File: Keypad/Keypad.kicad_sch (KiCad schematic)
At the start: 3 parts, among them J1 addon_conn

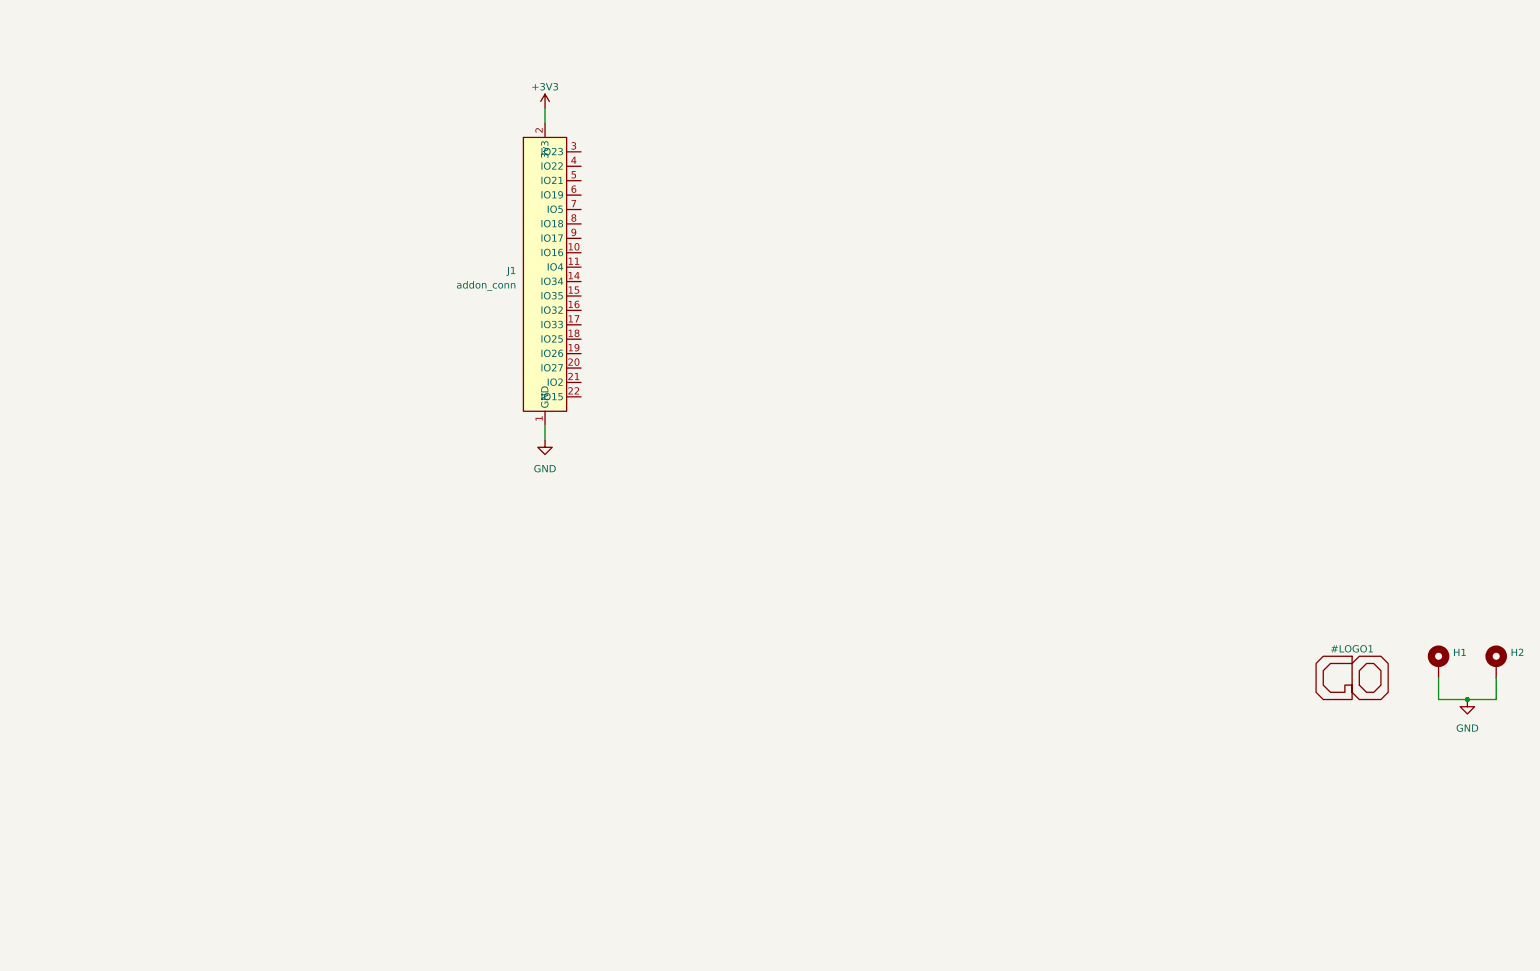
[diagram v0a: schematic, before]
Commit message: Adds schematics for keypad
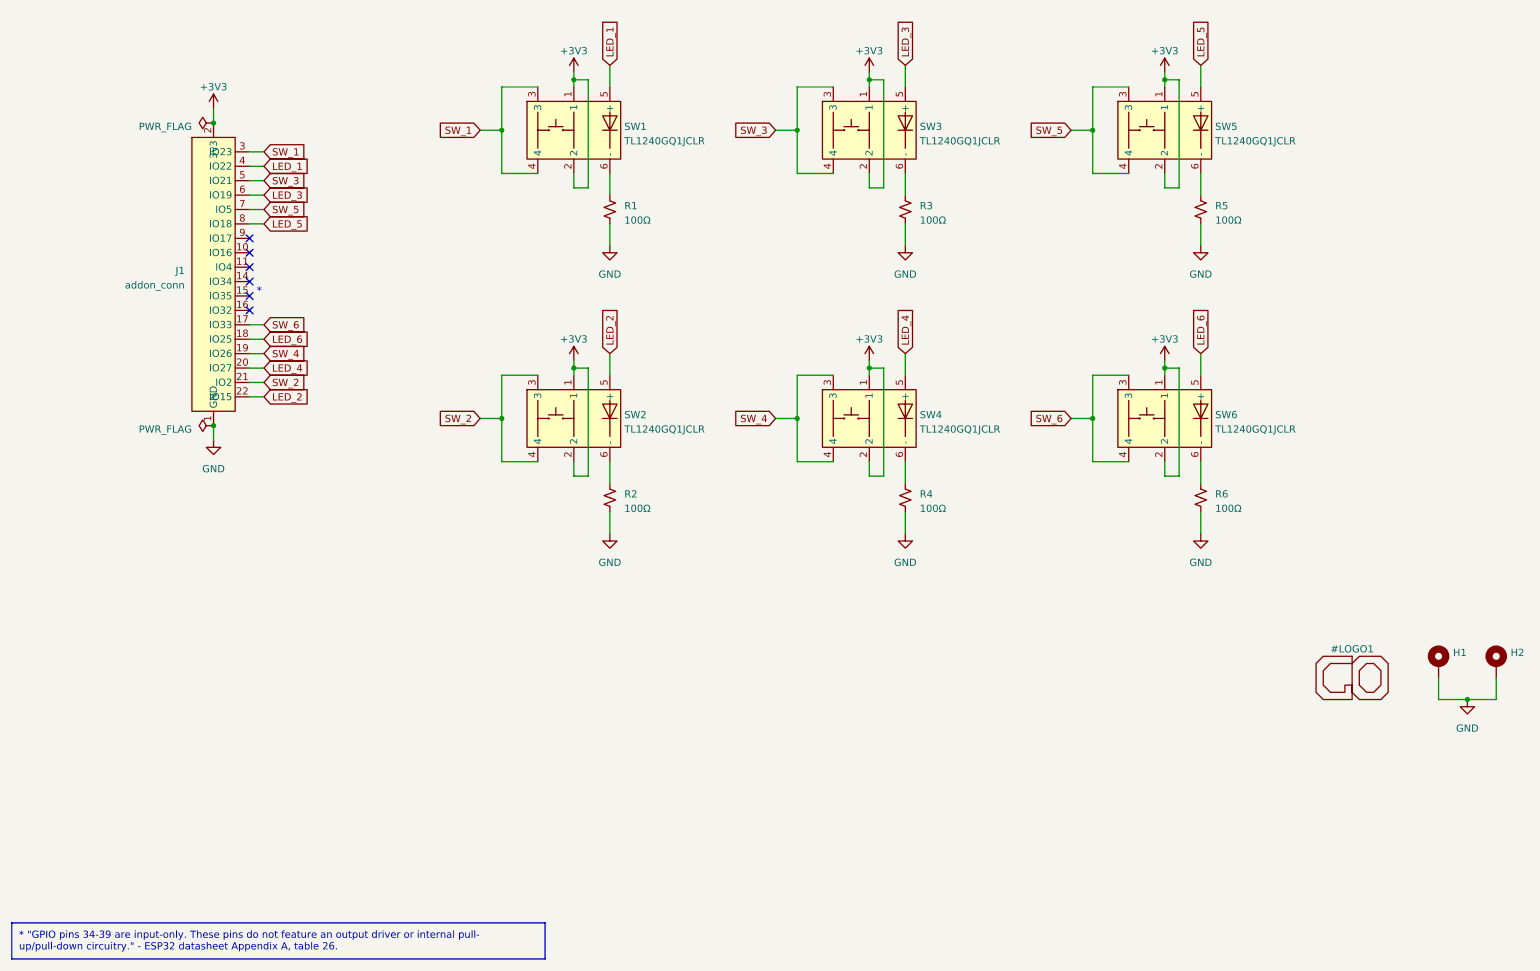
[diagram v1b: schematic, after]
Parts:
- added R1, R2, R3, R4, R5, R6: 100Ω, symbol Device:R_Small_US
- added SW1, SW2, SW3, SW4, SW5, SW6: TL1240GQ1JCLR, GameOver:TL1240GQ1JCLR, symbol GameOver:TL1240GQ1JCLR
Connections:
- net +3V3: now also SW1.1, SW1.2, SW2.1, SW2.2, SW3.1, SW3.2, SW4.1, SW4.2, SW5.1, SW5.2, SW6.1, SW6.2
- net GND: now also R1.2, R2.2, R3.2, R4.2, R5.2, R6.2
- net SW_6: now reaches J1.17 (IO33)
- net SW_6: now also SW6.3, SW6.4
- net LED_6: now reaches J1.18 (IO25)
- net LED_6: now also SW6.5 (+)
- net SW_4: now reaches J1.19 (IO26)
- net SW_4: now also SW4.3, SW4.4
- net LED_4: now reaches J1.20 (IO27)
- net LED_4: now also SW4.5 (+)
- net SW_2: now reaches J1.21 (IO2)
- net SW_2: now also SW2.3, SW2.4
- net LED_2: now reaches J1.22 (IO15)
- net LED_2: now also SW2.5 (+)
- net SW_1: now reaches J1.3 (IO23)
- net SW_1: now also SW1.3, SW1.4
- net LED_1: now reaches J1.4 (IO22)
- net LED_1: now also SW1.5 (+)
- net SW_3: now reaches J1.5 (IO21)
- net SW_3: now also SW3.3, SW3.4
- net LED_3: now reaches J1.6 (IO19)
- net LED_3: now also SW3.5 (+)
- net SW_5: now reaches J1.7 (IO5)
- net SW_5: now also SW5.3, SW5.4
- net LED_5: now reaches J1.8 (IO18)
- net LED_5: now also SW5.5 (+)
- new net: R1.1, SW1.6 (-)
- new net: R3.1, SW3.6 (-)
- new net: R6.1, SW6.6 (-)
- new net: R4.1, SW4.6 (-)
- new net: R5.1, SW5.6 (-)
- new net: R2.1, SW2.6 (-)
- no-connect marks 0 -> 6
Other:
- note added: "*"
- note added: "* "GPIO pins 34-39 are input-only. These pins do not feature an output driver or internal pull- up/pull-down circuitry." - ESP32 datasheet Appendix A, table 26."
- moved on the sheet: J1

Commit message: Only connects one of the pads for the buttons in keypad
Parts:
- R1, R2, R3, R4, R5, R6: footprint (none) -> Resistor_SMD:R_0805_2012Metric_Pad1.20x1.40mm_HandSolder
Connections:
- net SW_1: no longer SW1.3
- net SW_2: no longer SW2.4
- net SW_3: no longer SW3.3
- net SW_4: no longer SW4.4
- net SW_5: no longer SW5.3
- net SW_6: no longer SW6.4
- no-connect marks 6 -> 12

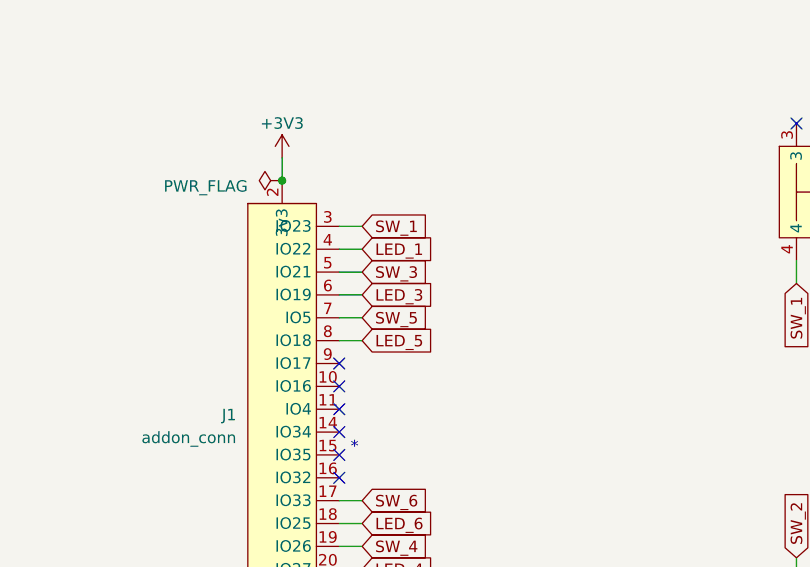
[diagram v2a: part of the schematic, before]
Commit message: Swaps switch and led pins for top row
This will make it easier to route the top buttons.
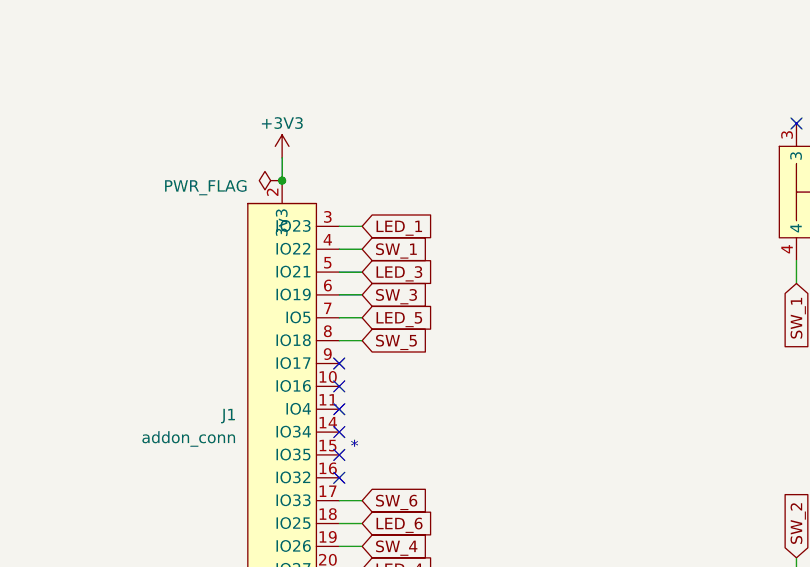
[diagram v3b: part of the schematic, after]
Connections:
- net LED_1: now also J1.3 (IO23); no longer J1.4 (IO22)
- net LED_3: now also J1.5 (IO21); no longer J1.6 (IO19)
- net LED_5: now also J1.7 (IO5); no longer J1.8 (IO18)
- net SW_1: now also J1.4 (IO22); no longer J1.3 (IO23)
- net SW_3: now also J1.6 (IO19); no longer J1.5 (IO21)
- net SW_5: now also J1.8 (IO18); no longer J1.7 (IO5)
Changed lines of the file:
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@@
     )
   )
-  (global_label "SW_1" (shape input) (at 59.69 52.07 0) (fields_autoplaced)
+  (global_label "SW_1" (shape input) (at 59.69 54.61 0) (fields_autoplaced)
     (effects (font (size 1.27 1.27)) (justify left))
-    (property "Intersheetrefs" "${INTERSHEET_REFS}" (id 0) (at 67.275 52.07 0)
+    (property "Intersheetrefs" "${INTERSHEET_REFS}" (id 0) (at 67.275 54.61 0)
       (effects (font (size 1.27 1.27)) (justify left) hide)
     )
@@
     )
   )
-  (global_label "SW_5" (shape input) (at 59.69 62.23 0) (fields_autoplaced)
+  (global_label "SW_5" (shape input) (at 59.69 64.77 0) (fields_autoplaced)
     (effects (font (size 1.27 1.27)) (justify left))
-    (property "Intersheetrefs" "${INTERSHEET_REFS}" (id 0) (at 67.275 62.23 0)
+    (property "Intersheetrefs" "${INTERSHEET_REFS}" (id 0) (at 67.275 64.77 0)
       (effects (font (size 1.27 1.27)) (justify left) hide)
     )
   )
-  (global_label "LED_5" (shape input) (at 59.69 64.77 0) (fields_autoplaced)
+  (global_label "LED_5" (shape input) (at 59.69 62.23 0) (fields_autoplaced)
     (effects (font (size 1.27 1.27)) (justify left))
-    (property "Intersheetrefs" "${INTERSHEET_REFS}" (id 0) (at 68.0612 64.77 0)
+    (property "Intersheetrefs" "${INTERSHEET_REFS}" (id 0) (at 68.0612 62.23 0)
       (effects (font (size 1.27 1.27)) (justify left) hide)
     )
@@
     )
   )
-  (global_label "LED_3" (shape input) (at 59.69 59.69 0) (fields_autoplaced)
+  (global_label "LED_3" (shape input) (at 59.69 57.15 0) (fields_autoplaced)
     (effects (font (size 1.27 1.27)) (justify left))
-    (property "Intersheetrefs" "${INTERSHEET_REFS}" (id 0) (at 68.0612 59.69 0)
+    (property "Intersheetrefs" "${INTERSHEET_REFS}" (id 0) (at 68.0612 57.15 0)
       (effects (font (size 1.27 1.27)) (justify left) hide)
     )
   )
-  (global_label "SW_3" (shape input) (at 59.69 57.15 0) (fields_autoplaced)
+  (global_label "SW_3" (shape input) (at 59.69 59.69 0) (fields_autoplaced)
     (effects (font (size 1.27 1.27)) (justify left))
-    (property "Intersheetrefs" "${INTERSHEET_REFS}" (id 0) (at 67.275 57.15 0)
+    (property "Intersheetrefs" "${INTERSHEET_REFS}" (id 0) (at 67.275 59.69 0)
       (effects (font (size 1.27 1.27)) (justify left) hide)
     )
@@
     )
   )
-  (global_label "LED_1" (shape input) (at 59.69 54.61 0) (fields_autoplaced)
+  (global_label "LED_1" (shape input) (at 59.69 52.07 0) (fields_autoplaced)
     (effects (font (size 1.27 1.27)) (justify left))
-    (property "Intersheetrefs" "${INTERSHEET_REFS}" (id 0) (at 68.0612 54.61 0)
+    (property "Intersheetrefs" "${INTERSHEET_REFS}" (id 0) (at 68.0612 52.07 0)
       (effects (font (size 1.27 1.27)) (justify left) hide)
     )

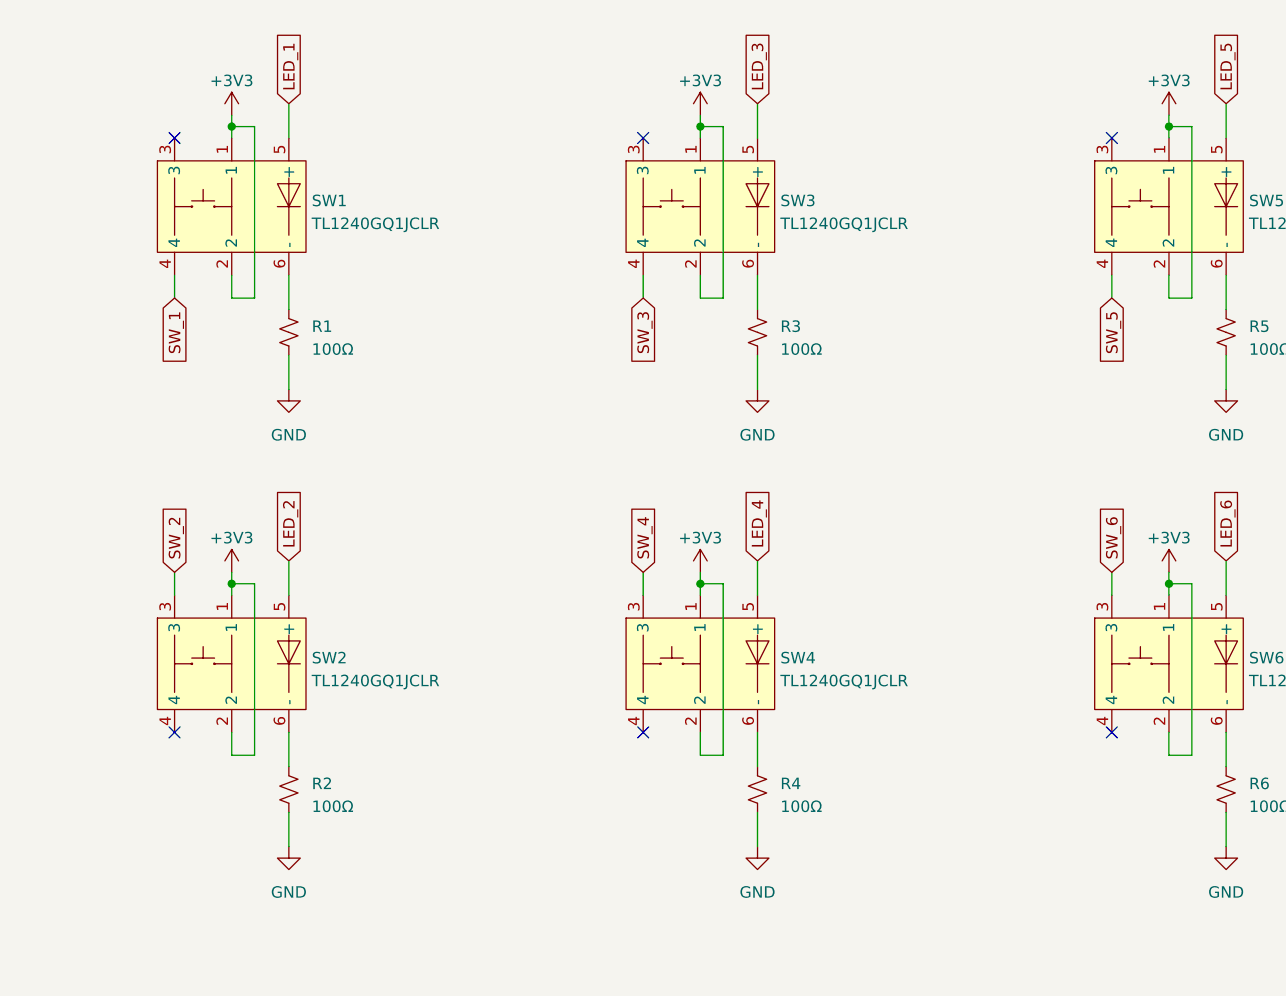
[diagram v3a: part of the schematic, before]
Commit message: Flips buttons on keypad
The keypad will have the same orientation as the Sensor board (with the
FFC connector on top). The buttons will be on the same side as the
connector.
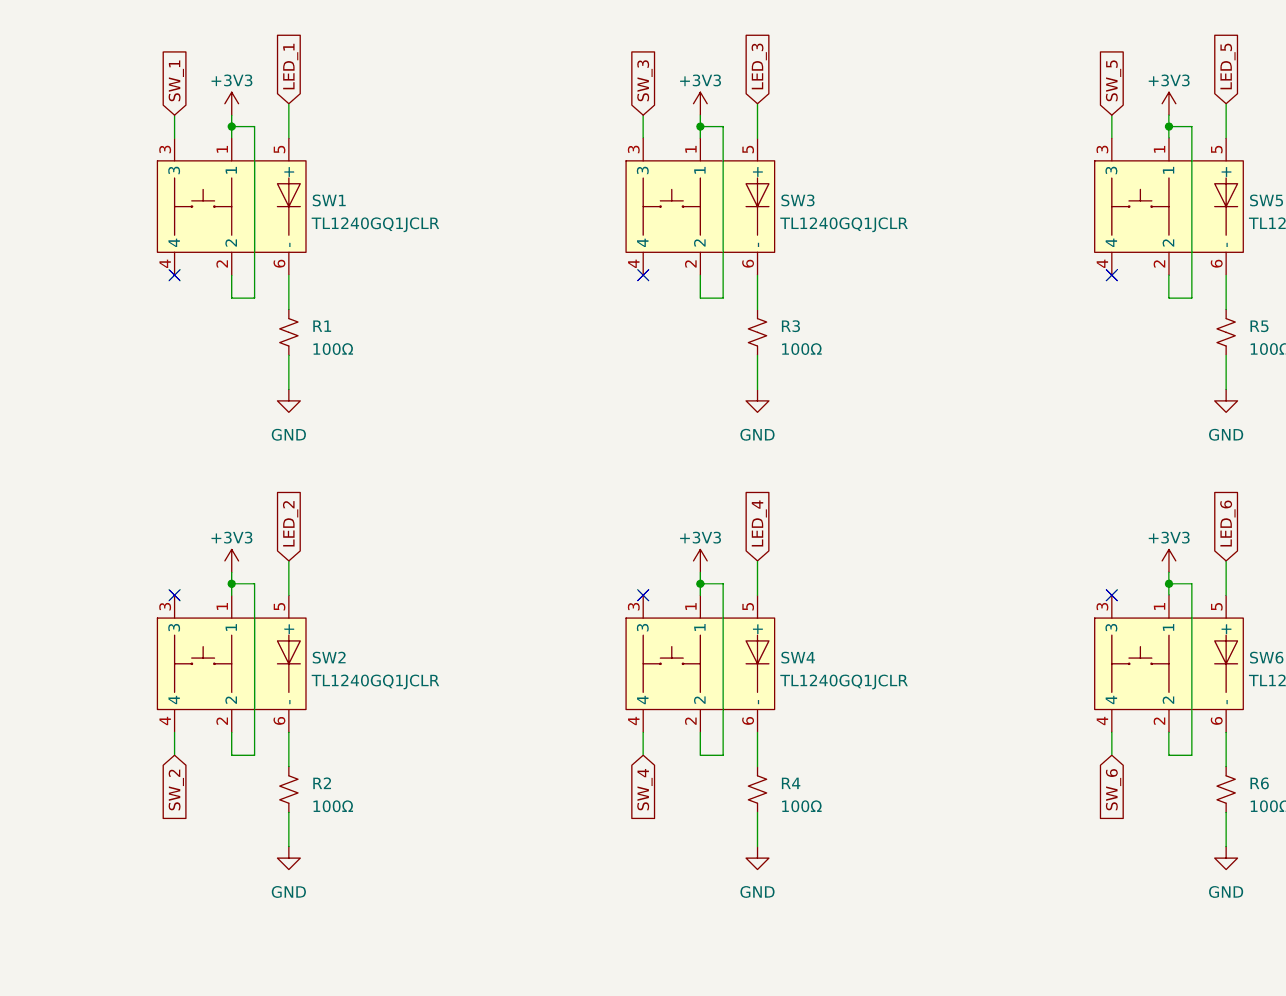
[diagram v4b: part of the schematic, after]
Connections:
- net SW_1: now also SW1.3; no longer SW1.4
- net SW_2: now also SW2.4; no longer SW2.3
- net SW_3: now also SW3.3; no longer SW3.4
- net SW_4: now also SW4.4; no longer SW4.3
- net SW_5: now also SW5.3; no longer SW5.4
- net SW_6: now also SW6.4; no longer SW6.3

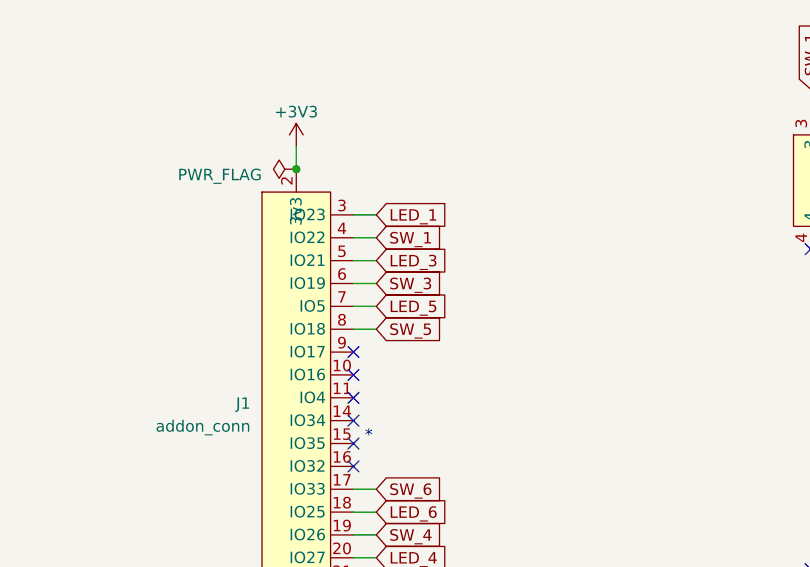
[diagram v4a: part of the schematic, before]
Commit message: Moves buttons a bit further away from screws
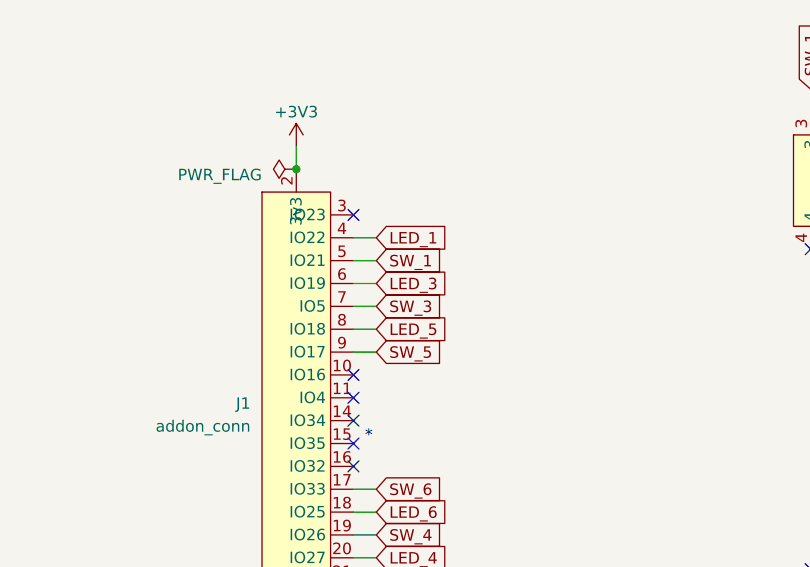
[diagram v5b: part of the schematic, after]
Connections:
- net LED_1: now also J1.4 (IO22); no longer J1.3 (IO23)
- net LED_3: now also J1.6 (IO19); no longer J1.5 (IO21)
- net LED_5: now also J1.8 (IO18); no longer J1.7 (IO5)
- net SW_1: now also J1.5 (IO21); no longer J1.4 (IO22)
- net SW_3: now also J1.7 (IO5); no longer J1.6 (IO19)
- net SW_5: now also J1.9 (IO17); no longer J1.8 (IO18)
